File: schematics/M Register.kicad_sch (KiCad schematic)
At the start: 26 parts, among them U20 74LS377, U21 74LS377, U22 74LS245, U23 74LS245

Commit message: schematics
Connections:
- net ML_OUT is gone; now on net M_OUT: U22.19 (CE)
- net MH_OUT renamed M_OUT
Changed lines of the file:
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@@
   (junction (at 147.32 52.07) (diameter 0) (color 0 0 0 0)
+  )
+  (junction (at 154.94 90.17) (diameter 0) (color 0 0 0 0)
   )
   (no_connect (at 160.02 124.46))
@@
     (stroke (width 0) (type default))
   )
-  (wire (pts (xy 160.02 74.93) (xy 157.48 74.93))
+  (wire (pts (xy 160.02 74.93) (xy 154.94 74.93))
     (stroke (width 0) (type default))
   )
@@
     (stroke (width 0) (type default))
   )
+  (wire (pts (xy 154.94 90.17) (xy 154.94 132.08))
+    (stroke (width 0) (type default))
+  )
   (wire (pts (xy 147.32 158.75) (xy 151.13 158.75))
     (stroke (width 0) (type default))
   )
+  (wire (pts (xy 154.94 90.17) (xy 46.99 90.17))
+    (stroke (width 0) (type default))
+  )
   (wire (pts (xy 185.42 106.68) (xy 196.85 106.68))
     (stroke (width 0) (type default))
@@
     (stroke (width 0) (type default))
   )
-  (wire (pts (xy 46.99 92.71) (xy 154.94 92.71))
-    (stroke (width 0) (type default))
-  )
   (wire (pts (xy 124.46 156.21) (xy 124.46 158.75))
     (stroke (width 0) (type default))
   )
-  (wire (pts (xy 154.94 92.71) (xy 154.94 132.08))
-    (stroke (width 0) (type default))
-  )
-  (wire (pts (xy 157.48 90.17) (xy 46.99 90.17))
-    (stroke (width 0) (type default))
-  )
   (wire (pts (xy 143.51 156.21) (xy 143.51 158.75))
     (stroke (width 0) (type default))
@@
     (stroke (width 0) (type default))
   )
-  (wire (pts (xy 157.48 74.93) (xy 157.48 90.17))
+  (wire (pts (xy 154.94 74.93) (xy 154.94 90.17))
     (stroke (width 0) (type default))
   )
@@
     (effects (font (size 1.27 1.27)) (justify left))
   )
-  (hierarchical_label "ML_OUT" (shape input) (at 46.99 90.17 180) (fields_autoplaced)
+  (hierarchical_label "M_OUT" (shape input) (at 46.99 90.17 180) (fields_autoplaced)
     (effects (font (size 1.27 1.27)) (justify right))
   )
@@
     (effects (font (size 1.27 1.27)) (justify left))
   )
-  (hierarchical_label "MH_OUT" (shape input) (at 46.99 92.71 180) (fields_autoplaced)
-    (effects (font (size 1.27 1.27)) (justify right))
-  )
   (symbol (lib_id "74xx:74LS245") (at 172.72 62.23 0) (unit 1)

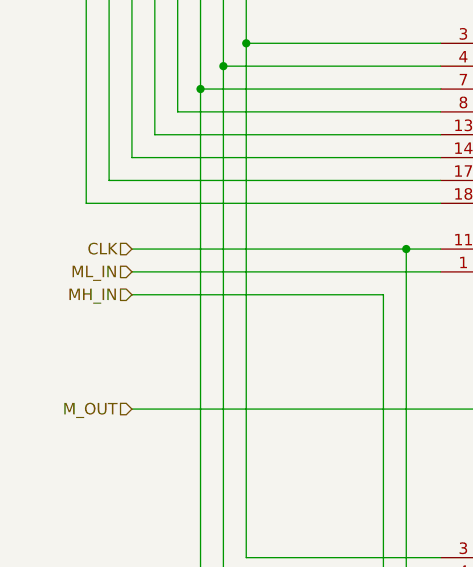
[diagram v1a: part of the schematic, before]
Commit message: control logic finished
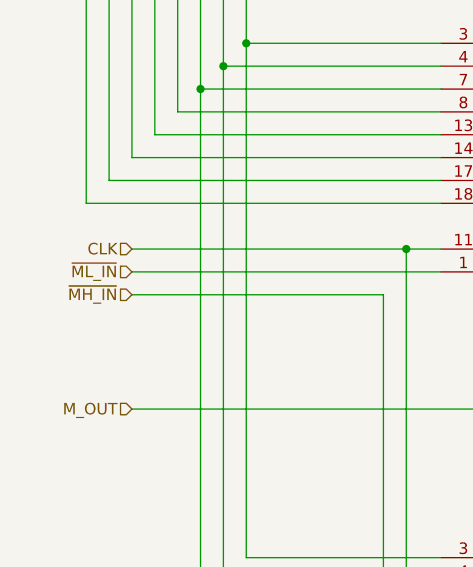
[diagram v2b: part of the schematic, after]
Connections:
- net MH_IN renamed ~{MH_IN}
- net ML_IN renamed ~{ML_IN}
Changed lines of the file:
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@@
     (effects (font (size 1.27 1.27)) (justify right))
   )
-  (hierarchical_label "ML_IN" (shape input) (at 46.99 74.93 180) (fields_autoplaced)
+  (hierarchical_label "~{ML_IN}" (shape input) (at 46.99 74.93 180) (fields_autoplaced)
     (effects (font (size 1.27 1.27)) (justify right))
   )
@@
     (effects (font (size 1.27 1.27)) (justify left))
   )
-  (hierarchical_label "MH_IN" (shape input) (at 46.99 77.47 180) (fields_autoplaced)
+  (hierarchical_label "~{MH_IN}" (shape input) (at 46.99 77.47 180) (fields_autoplaced)
     (effects (font (size 1.27 1.27)) (justify right))
   )
